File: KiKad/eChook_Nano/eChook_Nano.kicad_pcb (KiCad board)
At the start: 2 copper layers, 77 x 73.5 mm, 141 parts, among them J1 Expansion, U1 Arduino_Nano_v3.x, U2 TSR_1-2450, U3 MCP6002-xP, U4 ZXGD3009E6

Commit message: Fixed Mounting hole positions
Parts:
- R35: value 10k -> 16k
- moved H3 98.3 mm to (113.0, 132.2)
- moved H1 97.5 mm to (113.0, 66.7)
- moved H2 40.4 mm to (182.0, 66.7)
- moved H4 31.9 mm to (182.0, 132.2)
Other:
- board text added: "eChook nano V2.1 SMD 04/25"
- board text removed: "V2.0 SMD"
- board text removed: "eChook nano V2 SMD 10/24b"

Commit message: As Manufactured V2.1
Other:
- board text added: "JLCJLCJLCJLC"

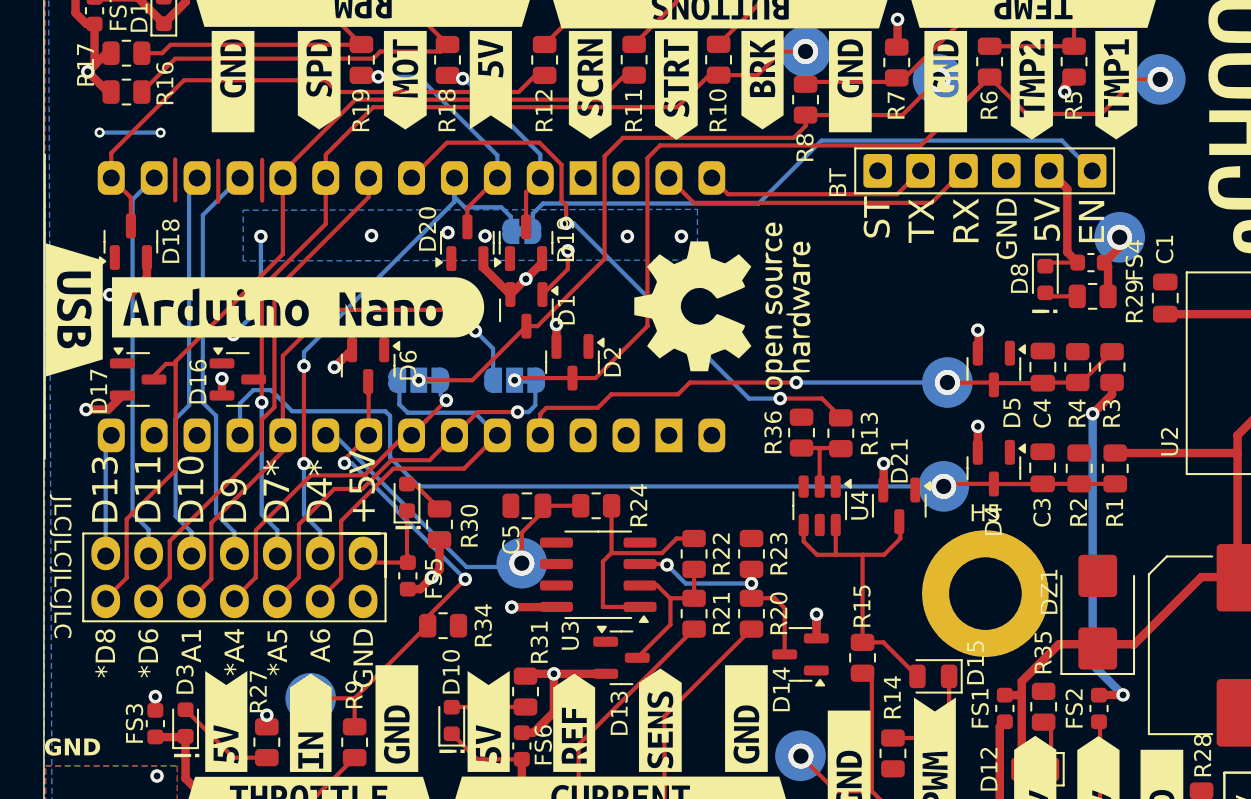
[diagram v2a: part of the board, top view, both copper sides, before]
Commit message: 24v LED fixed. Improved Routing and Labels
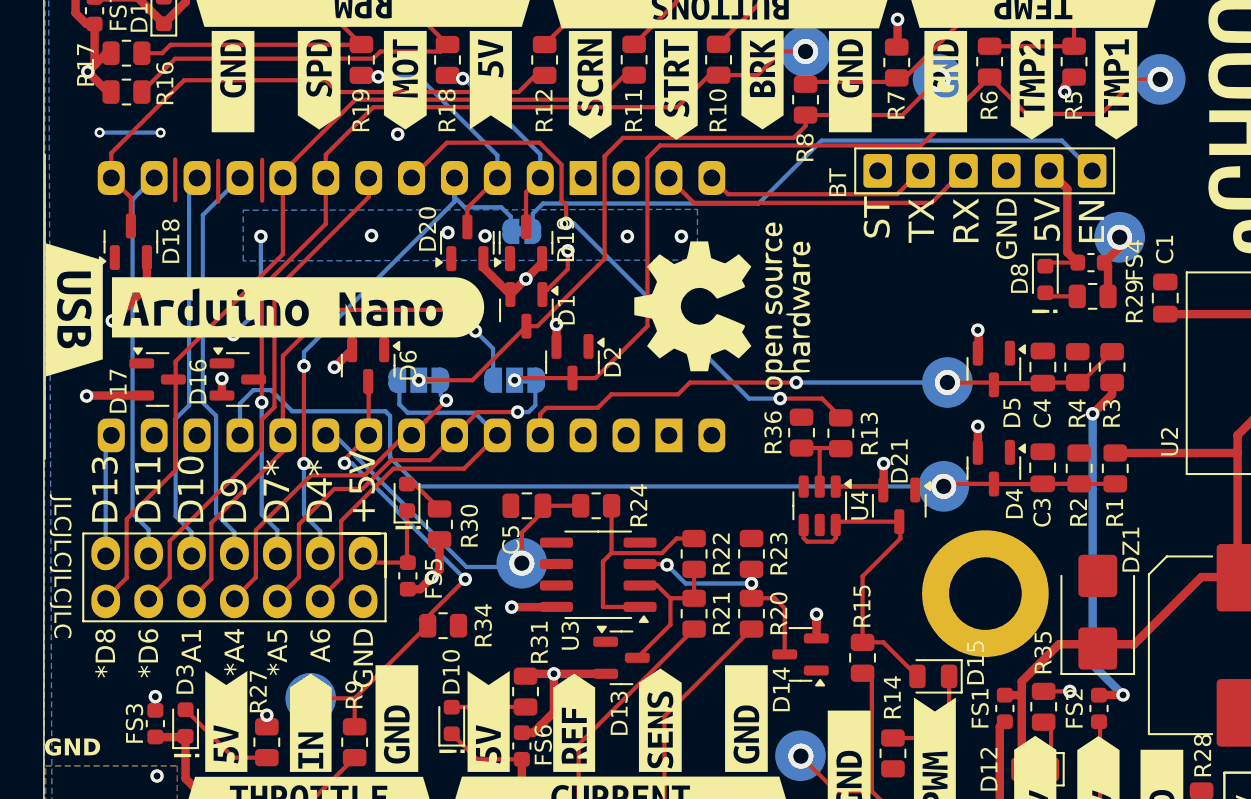
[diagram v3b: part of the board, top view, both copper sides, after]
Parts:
- moved D17 1.15 mm to (115.7, 98.1)
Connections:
- R35 pad 1: GND -> +5V
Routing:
- net +5V: track 63.5 -> 69.6 mm, vias 19 -> 20
- net /DriverButton: track 53.4 -> 51.9 mm
- net GND: vias 15 -> 17
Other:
- board text added: "12v"
- board text added: "BT EN"
- board text added: "Brk"
- board text added: "Btn1"
- board text added: "Btn2"
- board text added: "T1"
- board text added: "Temp / I2C"
- board text added: "Temp2"
- board text added: "Thtl"
- board text added: "Vbatt"
- board text added: "eChook nano V2.1.1 SMD 12/25"
- board text removed: "eChook nano V2.1 SMD 04/25"
